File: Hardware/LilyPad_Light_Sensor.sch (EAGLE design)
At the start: 9 parts, among them U1 TEMT6000

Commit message: Initial Commit
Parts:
- removed LIGHT+, LIGHT-, LIGHTS: SEWTAP6, LilyPad-Wearables:SEWTAP6
- removed LIGHT1, LIGHT2, LIGHT3: SEWTAP-NOHOLE2, LilyPad-Wearables:SEWTAP-NOHOLE2
- removed R1: 10K, SparkFun:RESISTOR0402
- removed U$2: LOGO-LPLP, LilyPad-Wearables:LOGO-LPLP
- removed U1: TEMT6000, SparkFun:TEMT6000
- added FRAME2: FRAME-LETTER, SparkFun-Aesthetics:FRAME-LETTER
- added R24: 10k, SparkFun-Resistors:10KOHM-0603-1/10W-1%
- added SEWTAPLS+: PLUS, LilyPad-Wearables:SEWTAP_SMALL-2SIDE
- added SEWTAPLS-: MINUS, LilyPad-Wearables:SEWTAP_SMALL-2SIDE
- added SEWTAPLSOUT: OUT, LilyPad-Wearables:SEWTAP_SMALL-2SIDE
- added ST1, ST2, ST3: SEWTAP-NOHOLE_SM_NH, LilyPad-Wearables:SEWTAP-NOHOLE_SM_NH
- added U$1: SPECIAL_INSTRUCTIONS-ORDERING, SparkFun-Aesthetics:SPECIAL_INSTRUCTIONS-ORDERING
- added U3: ALS-PT19, SparkFun-Sensors:LIGHT_SENSORALS
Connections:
- removed net +: LIGHT+.1, U1.C1
- removed net -: LIGHT-.1, R1.1
- removed net S: LIGHTS.1, R1.2, U1.E1
- new net 3.3V: SEWTAPLS+.1, U3.C1
- new net D2: R24.2, SEWTAPLSOUT.1, U3.E1
- new net GND: R24.1, SEWTAPLS-.1
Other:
- note added: "Light Sensor"
- note added: "Marshall Taylor"
- note added: "Un-used sew taps"
- note added: "v10"
- note removed: "Lilypad - Light Sensor"
- note removed: "v13"

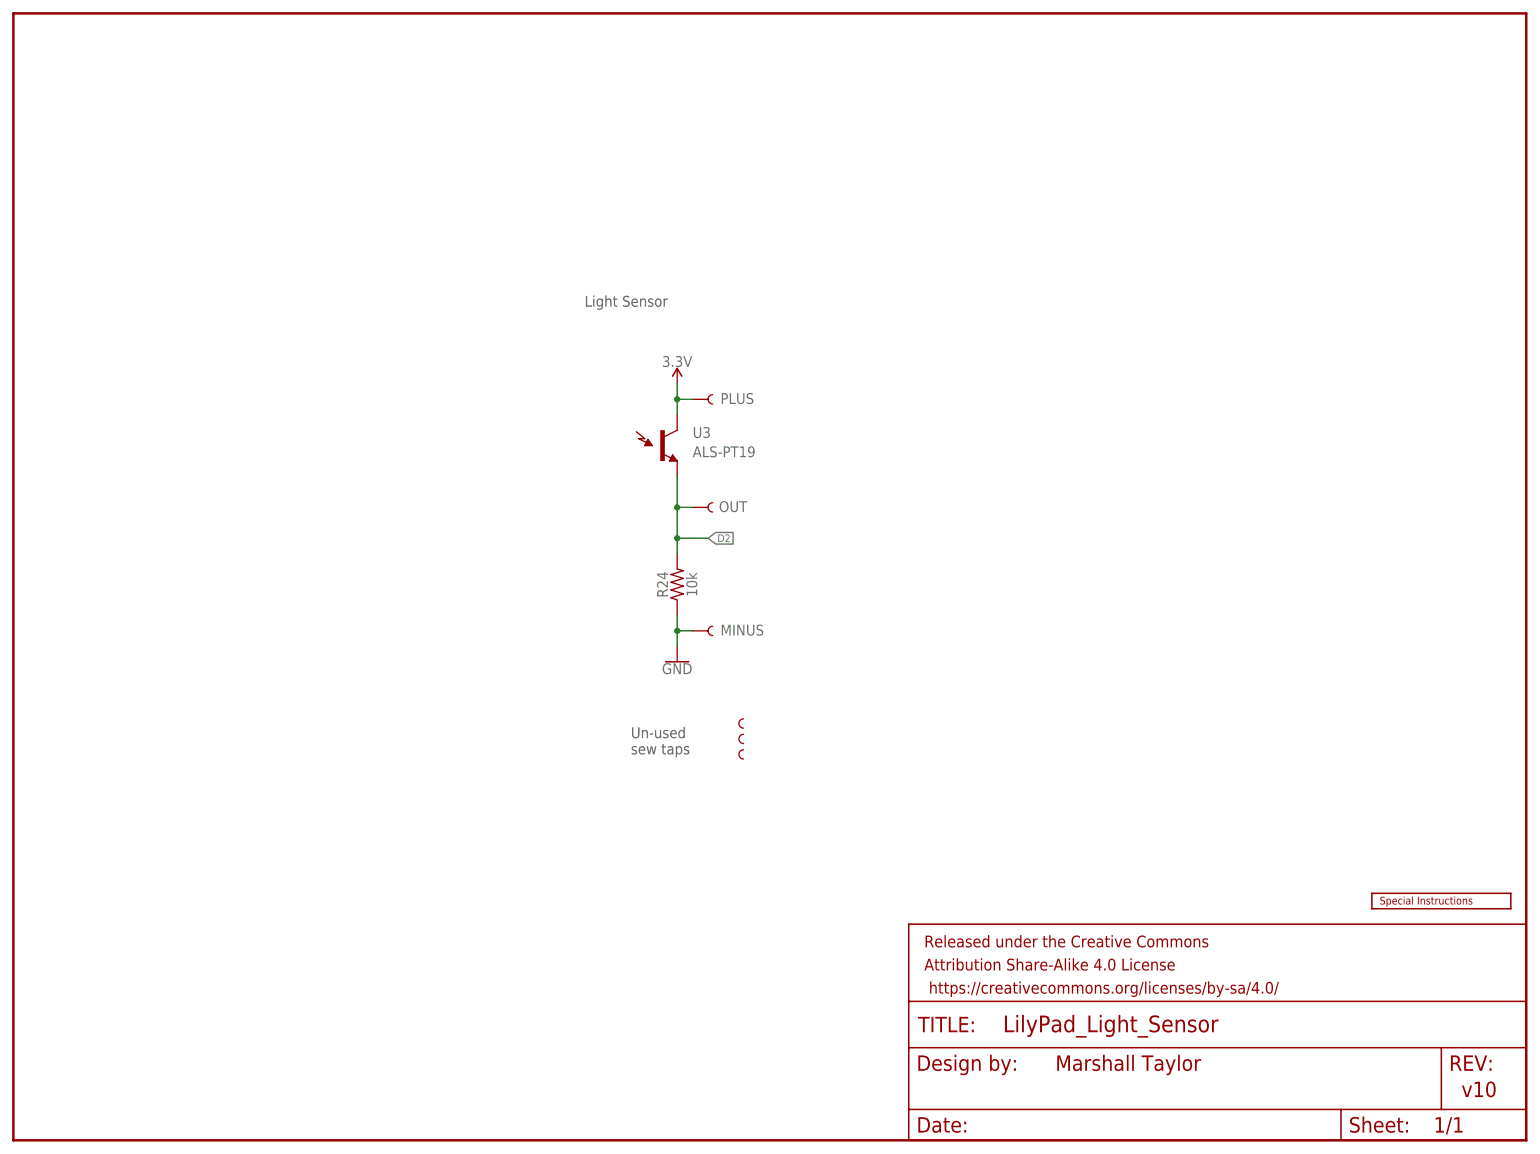
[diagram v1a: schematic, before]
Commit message: Small changes after review
"Revised by:" added to schematic and version number fixed.
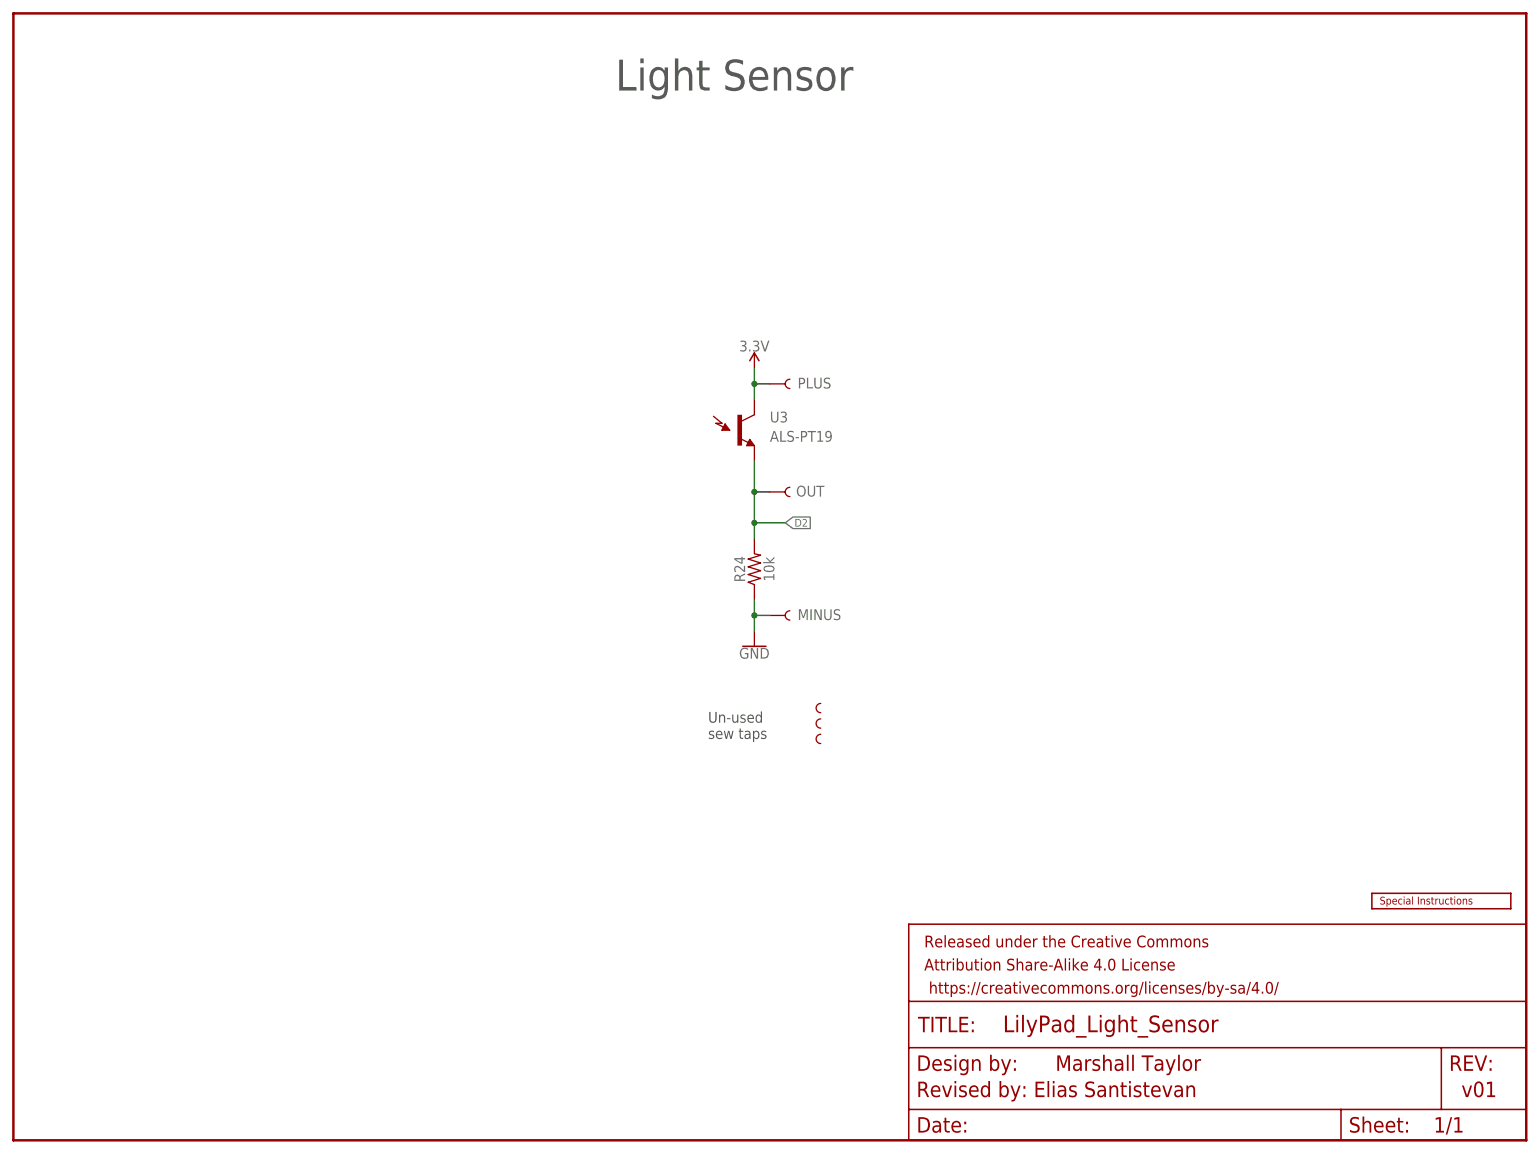
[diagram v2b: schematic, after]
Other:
- note added: "Revised by: Elias Santistevan"
- note added: "v01"
- note removed: "v10"
- moved on the sheet: R24, U3
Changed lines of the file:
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@@
 <sheet>
 <plain>
-<text x="101.6" y="63.5" size="1.778" layer="97">Un-used
+<text x="114.3" y="66.04" size="1.778" layer="97">Un-used
 sew taps</text>
-<text x="93.98" y="137.16" size="1.778" layer="97">Light Sensor</text>
+<text x="99.06" y="172.72" size="5.08" layer="97">Light Sensor</text>
 <text x="171.45" y="11.43" size="2.54" layer="94">Marshall Taylor</text>
-<text x="238.252" y="7.112" size="2.54" layer="94">v10</text>
+<text x="238.252" y="7.112" size="2.54" layer="94">v01</text>
+<text x="148.59" y="7.112" size="2.54" layer="94">Revised by: Elias Santistevan</text>
 </plain>
 <instances>
-<instance part="ST3" gate="G$1" x="119.38" y="63.5" smashed="yes"/>
-<instance part="ST2" gate="G$1" x="119.38" y="66.04" smashed="yes"/>
-<instance part="ST1" gate="G$1" x="119.38" y="68.58" smashed="yes"/>
-<instance part="SEWTAPLS-" gate="G$1" x="114.3" y="83.82" smashed="yes">
-<attribute name="VALUE" x="116.332" y="83.058" size="1.778" layer="96"/>
+<instance part="ST3" gate="G$1" x="132.08" y="66.04" smashed="yes"/>
+<instance part="ST2" gate="G$1" x="132.08" y="68.58" smashed="yes"/>
+<instance part="ST1" gate="G$1" x="132.08" y="71.12" smashed="yes"/>
+<instance part="SEWTAPLS-" gate="G$1" x="127" y="86.36" smashed="yes">
+<attribute name="VALUE" x="129.032" y="85.598" size="1.778" layer="96"/>
 </instance>
-<instance part="SEWTAPLS+" gate="G$1" x="114.3" y="121.92" smashed="yes">
-<attribute name="VALUE" x="116.332" y="121.158" size="1.778" layer="96"/>
+<instance part="SEWTAPLS+" gate="G$1" x="127" y="124.46" smashed="yes">
+<attribute name="VALUE" x="129.032" y="123.698" size="1.778" layer="96"/>
 </instance>
-<instance part="SEWTAPLSOUT" gate="G$1" x="114.3" y="104.14" smashed="yes">
-<attribute name="VALUE" x="116.078" y="103.378" size="1.778" layer="96"/>
+<instance part="SEWTAPLSOUT" gate="G$1" x="127" y="106.68" smashed="yes">
+<attribute name="VALUE" x="128.778" y="105.918" size="1.778" layer="96"/>
 </instance>
-<instance part="R24" gate="G$1" x="109.22" y="91.44" rot="R90"/>
-<instance part="U3" gate="G$1" x="106.68" y="114.3" smashed="yes">
-<attribute name="VALUE" x="111.76" y="112.395" size="1.778" layer="96"/>
-<attribute name="NAME" x="111.76" y="115.57" size="1.778" layer="95"/>
+<instance part="R24" gate="G$1" x="121.92" y="93.98" rot="R90"/>
+<instance part="U3" gate="G$1" x="119.38" y="116.84" smashed="yes">
+<attribute name="VALUE" x="124.46" y="114.935" size="1.778" layer="96"/>
+<attribute name="NAME" x="124.46" y="118.11" size="1.778" layer="95"/>
 </instance>
-<instance part="P+8" gate="G$1" x="109.22" y="124.46"/>
-<instance part="GND24" gate="1" x="109.22" y="78.74"/>
+<instance part="P+8" gate="G$1" x="121.92" y="127"/>
+<instance part="GND24" gate="1" x="121.92" y="81.28"/>
 <instance part="FRAME2" gate="G$1" x="0" y="0"/>
 <instance part="FRAME2" gate="V" x="147.32" y="0"/>
@@
 <pinref part="SEWTAPLS-" gate="G$1" pin="1"/>
 <pinref part="R24" gate="G$1" pin="1"/>
-<wire x1="109.22" y1="86.36" x2="109.22" y2="83.82" width="0.1524" layer="91"/>
-<wire x1="109.22" y1="83.82" x2="111.76" y2="83.82" width="0.1524" layer="91"/>
-<wire x1="109.22" y1="83.82" x2="109.22" y2="81.28" width="0.1524" layer="91"/>
-<junction x="109.22" y="83.82"/>
+<wire x1="121.92" y1="88.9" x2="121.92" y2="86.36" width="0.1524" layer="91"/>
+<wire x1="121.92" y1="86.36" x2="124.46" y2="86.36" width="0.1524" layer="91"/>
+<wire x1="121.92" y1="86.36" x2="121.92" y2="83.82" width="0.1524" layer="91"/>
+<junction x="121.92" y="86.36"/>
 <pinref part="GND24" gate="1" pin="GND"/>
 </segment>
@@
 <pinref part="SEWTAPLS+" gate="G$1" pin="1"/>
 <pinref part="U3" gate="G$1" pin="C1"/>
-<wire x1="109.22" y1="119.38" x2="109.22" y2="121.92" width="0.1524" layer="91"/>
-<wire x1="109.22" y1="121.92" x2="111.76" y2="121.92" width="0.1524" layer="91"/>
-<wire x1="109.22" y1="121.92" x2="109.22" y2="124.46" width="0.1524" layer="91"/>
-<junction x="109.22" y="121.92"/>
+<wire x1="121.92" y1="121.92" x2="121.92" y2="124.46" width="0.1524" layer="91"/>
+<wire x1="121.92" y1="124.46" x2="124.46" y2="124.46" width="0.1524" layer="91"/>
+<wire x1="121.92" y1="124.46" x2="121.92" y2="127" width="0.1524" layer="91"/>
+<junction x="121.92" y="124.46"/>
 <pinref part="P+8" gate="G$1" pin="3.3V"/>
 </segment>
@@
 <net name="D2" class="0">
 <segment>
-<wire x1="109.22" y1="96.52" x2="109.22" y2="99.06" width="0.1524" layer="91"/>
-<wire x1="109.22" y1="99.06" x2="109.22" y2="104.14" width="0.1524" layer="91"/>
+<wire x1="121.92" y1="99.06" x2="121.92" y2="101.6" width="0.1524" layer="91"/>
+<wire x1="121.92" y1="101.6" x2="121.92" y2="106.68" width="0.1524" layer="91"/>
 <pinref part="SEWTAPLSOUT" gate="G$1" pin="1"/>
 <pinref part="R24" gate="G$1" pin="2"/>
 <pinref part="U3" gate="G$1" pin="E1"/>
-<wire x1="109.22" y1="104.14" x2="109.22" y2="109.22" width="0.1524" layer="91"/>
-<junction x="109.22" y="99.06"/>
-<wire x1="111.76" y1="104.14" x2="109.22" y2="104.14" width="0.1524" layer="91"/>
-<junction x="109.22" y="104.14"/>
-<wire x1="109.22" y1="99.06" x2="114.3" y2="99.06" width="0.1524" layer="91"/>
-<label x="114.3" y="99.06" size="1.27" layer="95" xref="yes"/>
+<wire x1="121.92" y1="106.68" x2="121.92" y2="111.76" width="0.1524" layer="91"/>
+<junction x="121.92" y="101.6"/>
+<wire x1="124.46" y1="106.68" x2="121.92" y2="106.68" width="0.1524" layer="91"/>
+<junction x="121.92" y="106.68"/>
+<wire x1="121.92" y1="101.6" x2="127" y2="101.6" width="0.1524" layer="91"/>
+<label x="127" y="101.6" size="1.27" layer="95" xref="yes"/>
 </segment>
 </net>

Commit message: Fiducials, VCC Range added
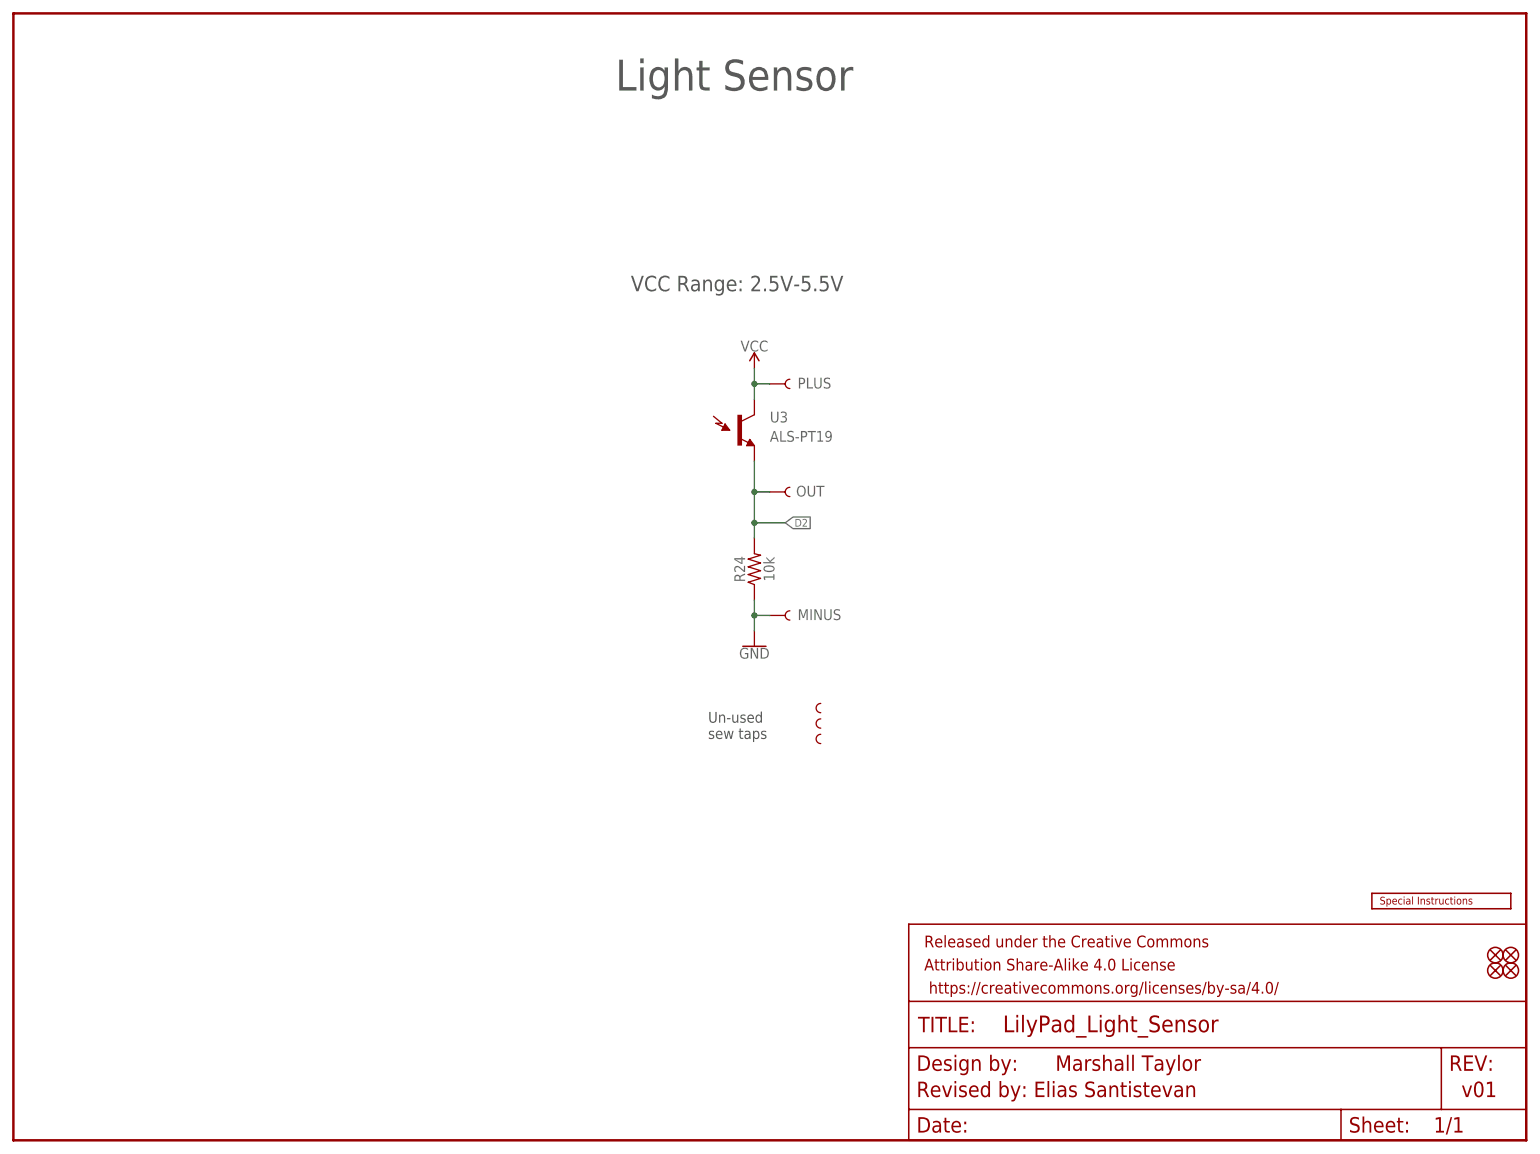
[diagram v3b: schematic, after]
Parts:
- added FD1, FD2, FD3, FD4: FIDUCIALUFIDUCIAL, SparkFun-Aesthetics:FIDUCIALUFIDUCIAL
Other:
- note added: "VCC Range: 2.5V-5.5V"
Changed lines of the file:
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@@
 <part name="R24" library="SparkFun-Resistors" deviceset="10KOHM" device="-0603-1/10W-1%" value="10k"/>
 <part name="U3" library="SparkFun-Sensors" deviceset="LIGHT_SENSOR" device="ALS" value="ALS-PT19"/>
-<part name="P+8" library="SparkFun-PowerSymbols" deviceset="3.3V" device=""/>
+<part name="P+8" library="SparkFun-PowerSymbols" deviceset="VCC" device=""/>
 <part name="GND24" library="SparkFun-PowerSymbols" deviceset="GND" device=""/>
 <part name="FRAME2" library="SparkFun-Aesthetics" deviceset="FRAME-LETTER" device="" value="FRAME-LETTER"/>
 <part name="U$1" library="SparkFun-Aesthetics" deviceset="SPECIAL_INSTRUCTIONS" device="-ORDERING"/>
+<part name="FD1" library="SparkFun-Aesthetics" deviceset="FIDUCIAL" device="UFIDUCIAL"/>
+<part name="FD2" library="SparkFun-Aesthetics" deviceset="FIDUCIAL" device="UFIDUCIAL"/>
+<part name="FD3" library="SparkFun-Aesthetics" deviceset="FIDUCIAL" device="UFIDUCIAL"/>
+<part name="FD4" library="SparkFun-Aesthetics" deviceset="FIDUCIAL" device="UFIDUCIAL"/>
 </parts>
 <sheets>
@@
 <text x="238.252" y="7.112" size="2.54" layer="94">v01</text>
 <text x="148.59" y="7.112" size="2.54" layer="94">Revised by: Elias Santistevan</text>
+<text x="101.6" y="139.7" size="2.54" layer="97">VCC Range: 2.5V-5.5V</text>
 </plain>
 <instances>
@@
 <instance part="FRAME2" gate="V" x="147.32" y="0"/>
 <instance part="U$1" gate="G$1" x="223.52" y="38.1"/>
+<instance part="FD1" gate="G$1" x="246.38" y="30.48"/>
+<instance part="FD2" gate="G$1" x="243.84" y="30.48"/>
+<instance part="FD3" gate="G$1" x="243.84" y="27.94"/>
+<instance part="FD4" gate="G$1" x="246.38" y="27.94"/>
 </instances>
 <busses>
@@
 <wire x1="121.92" y1="124.46" x2="121.92" y2="127" width="0.1524" layer="91"/>
 <junction x="121.92" y="124.46"/>
-<pinref part="P+8" gate="G$1" pin="3.3V"/>
+<pinref part="P+8" gate="G$1" pin="VCC"/>
 </segment>
 </net>
